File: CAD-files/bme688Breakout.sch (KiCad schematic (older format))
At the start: 9 parts, among them J1 Conn_01x04_Male, U1 BME688

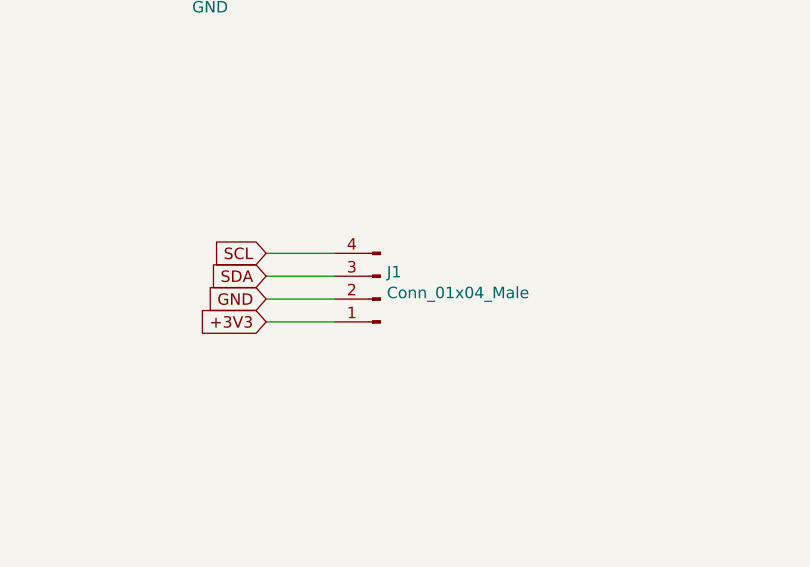
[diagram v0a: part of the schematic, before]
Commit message: added castellated holes
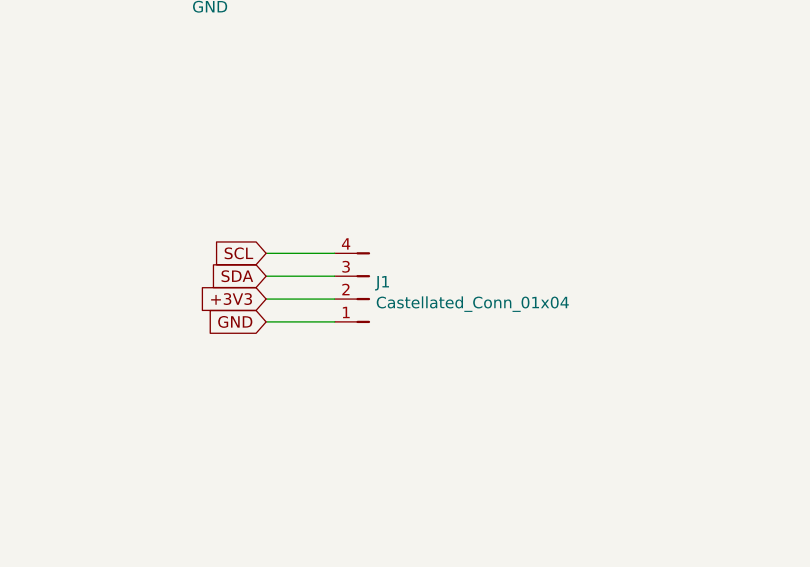
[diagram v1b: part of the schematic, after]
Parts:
- removed J1: Conn_01x04_Male, Connector_PinHeader_2.54mm:PinHeader_1x04_P2.54mm_Vertical, symbol Connector:Conn_01x04_Male
- added J1: Castellated_Conn_01x04, DS-connectors:Castellated_PinHeader_01x04_P2.54mm_Vertical, symbol DS-connectors:Castellated_Conn_01x04
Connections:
- net +3V3: now also J1.2
- net GND: now also J1.1
- net SCL: now also J1.4
- net SDA: now also J1.3
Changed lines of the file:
@@
 Wire Wire Line
 	7500 2600 7500 2700
-$Comp
-L Connector:Conn_01x04_Male J1
-U 1 1 61417FC7
-P 8250 4150
-F 0 "J1" H 8222 4032 50  0000 R CNN
-F 1 "Conn_01x04_Male" H 8222 4123 50  0000 R CNN
-F 2 "Connector_PinHeader_2.54mm:PinHeader_1x04_P2.54mm_Vertical" H 8250 4150 50  0001 C CNN
-F 3 "~" H 8250 4150 50  0001 C CNN
-	1    8250 4150
-	-1   0    0    1
-$EndComp
 Text GLabel 7750 3950 0    50   Input ~ 0
 SCL
@@
 SDA
 Text GLabel 7750 4150 0    50   Input ~ 0
++3V3
+Text GLabel 7750 4250 0    50   Input ~ 0
 GND
-Text GLabel 7750 4250 0    50   Input ~ 0
-+3V3
 Wire Wire Line
 	7750 3950 8050 3950
@@
 Wire Wire Line
 	3950 4100 4350 4100
+$Comp
+L DS-connectors:Castellated_Conn_01x04 J1
+U 1 1 6153419D
+P 8200 4300
+F 0 "J1" H 8170 4076 50  0000 R CNN
+F 1 "Castellated_Conn_01x04" H 8170 4167 50  0000 R CNN
+F 2 "DS-connectors:Castellated_PinHeader_01x04_P2.54mm_Vertical" H 8200 4300 50  0001 C CNN
+F 3 "" H 8200 4300 50  0001 C CNN
+	1    8200 4300
+	-1   0    0    1
+$EndComp
 $EndSCHEMATC

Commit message: Add files via upload
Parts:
- added J2, J3: Castellated_Conn_01x01, DS-connectors:Castellated_PinHeader_01x01_P2.54mm_Vertical, symbol DS-connectors:Castellated_Conn_01x01
- C1, C2: footprint Capacitor_SMD:C_0603_1608Metric -> Capacitor_SMD:C_0805_2012Metric
- R1, R2, R3, R4: footprint Resistor_SMD:R_0603_1608Metric -> Resistor_SMD:R_0805_2012Metric
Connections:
- net GND: now also J2.1, J3.1
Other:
- note removed: "01"
- note removed: "09/13/2021"
- note removed: "BME680/688 Breakout Board"
- moved on the sheet: C1, C2, J1, JP1, R1, R2, R3, R4, U1
